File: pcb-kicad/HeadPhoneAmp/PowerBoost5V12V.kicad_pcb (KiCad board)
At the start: 2 copper layers, 36.7 x 23.6 mm, 39 parts, among them Q1 Q_PNP_ECB_BRT, U1 VREG_TPS6103X, U2 MCP73871

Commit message: Added some order infos.
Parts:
- B1: value BATTERY -> ~
- C1: value 10u -> 2.2u
- C6: value C-USC1210 -> 22u
- CHRG/LBO0, DONE0, LED2: value LED0805_NOOUTLINE -> ~
- JP2: value HEADER-1X8ROUND -> ~
- LED1: value LOW-BAT -> ~
- R16: value 2k -> 1k
- TP1, TP3, TP5: value GND -> ~
- TP2: value 5V -> ~
- TP4: value PAD -> ~

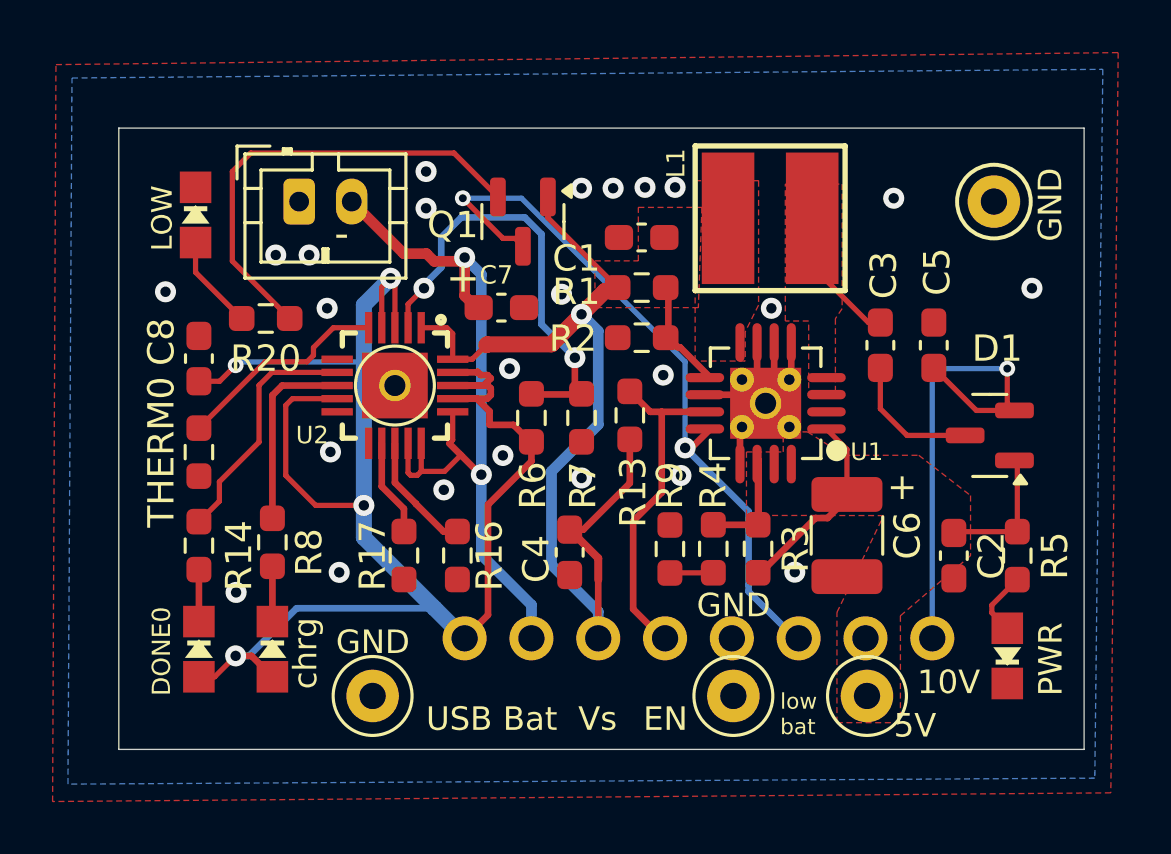
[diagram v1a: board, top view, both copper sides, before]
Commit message: Fixed PowerBlock PCB it's v0.2 now
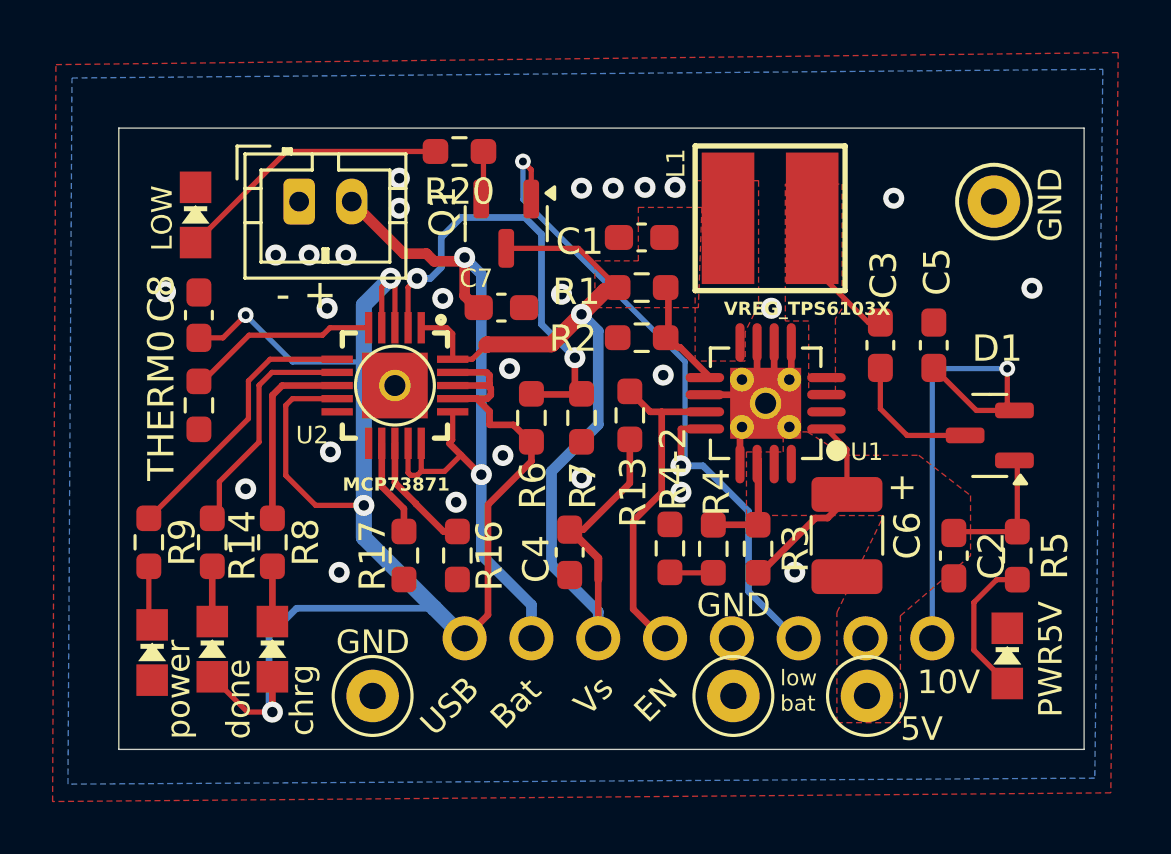
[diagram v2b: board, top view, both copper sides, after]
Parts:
- added LEDPG1: PG, Adafruit PowerBoost 1000C Rev B:CHIPLED_0805_NOOUTLINE, F.Cu at (131.4, 113.2)
- added R4-2: 100k, Resistor_SMD:R_0603_1608Metric_Pad0.98x0.95mm_HandSolder, F.Cu at (151.1, 109.2)
- Q1: value Q_PNP_ECB_BRT -> Q_PNP_BEC_BRT
- R9: value 100k -> 1k
- moved R9 19.8 mm to (131.3, 109.0)
- moved R20 9.73 mm to (143.1, 94.1)
- moved THERM0 1.78 mm to (133.2, 103.8)
- moved C8 1.65 mm to (133.2, 100.3)
- moved Q1 0.64 mm to (144.9, 96.9)
- moved R14 0.52 mm to (133.7, 109.0)
- moved DONE0 0.51 mm to (133.7, 113.0)
- turned LED2 to 0 degrees
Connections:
- Q1 pad 1: VBAT -> /LBO
- Q1 pad 3: /LBO -> VBAT
- R4 pad 1: Net-(R4-Pad1) -> Net-(R4-2-Pad2)
- R9 pad 1: GND -> Net-(U2-/PG)
- R9 pad 2: Net-(R4-Pad1) -> Net-(LEDPG1-PadC)
- U2 pad P$6: unconnected-(U2-/PG-PadP$6) -> Net-(U2-/PG)
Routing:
- net Net-(Q1-E): track 17.6 -> 1.84 mm
- net Net-(U2-/PG): track 0.00 -> 10.5 mm
- net Net-(LED1-PadA): track 3.61 -> 10.6 mm
- net Net-(LED2-PadA): track 2.49 -> 5.62 mm
- net Net-(LEDPG1-PadC): track 0.00 -> 2.28 mm
- net Net-(R4-Pad1): track 1.65 -> 0.00 mm
- net Net-(R4-2-Pad2): track 0.00 -> 1.65 mm
- net VBUS: track 65.3 -> 66.9 mm
- net Net-(U2-THERM): track 8.21 -> 7.30 mm
- net GND: vias 24 -> 26
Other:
- board text added: "- +"
- board text added: "PWR5V"
- board text added: "done"
- board text added: "mb'PowerBoost v0.2"
- board text added: "power"
- board text removed: "-"
- board text removed: "PWR"
- board text removed: "mb'PowerBoost v0.1"
